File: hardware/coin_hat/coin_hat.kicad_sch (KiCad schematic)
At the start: 45 parts, among them J1 Pi 40-pin (bottom side), J10 Coin sensor, J11 Aux header, J12 Aux 12V switched, J2 Belt motor, J3 Feeder motor, J4 Diverter motor, J5 12 V in 5.5/2.1, J6 LED ring (WS2812), J7 Key light 12V switched, J8 Home: diverter, J9 Home: feeder, Q1 AO3400, Q2 AO3400, Q3 AO3400, U1 Raspberry Pi Pico, U2 TMC2209 StepStick, U3 TMC2209 StepStick, U4 TMC2209 StepStick, U5 12V->5V 5A module (Pololu D24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, U6 74AHCT1G125, U7 CAT24C32

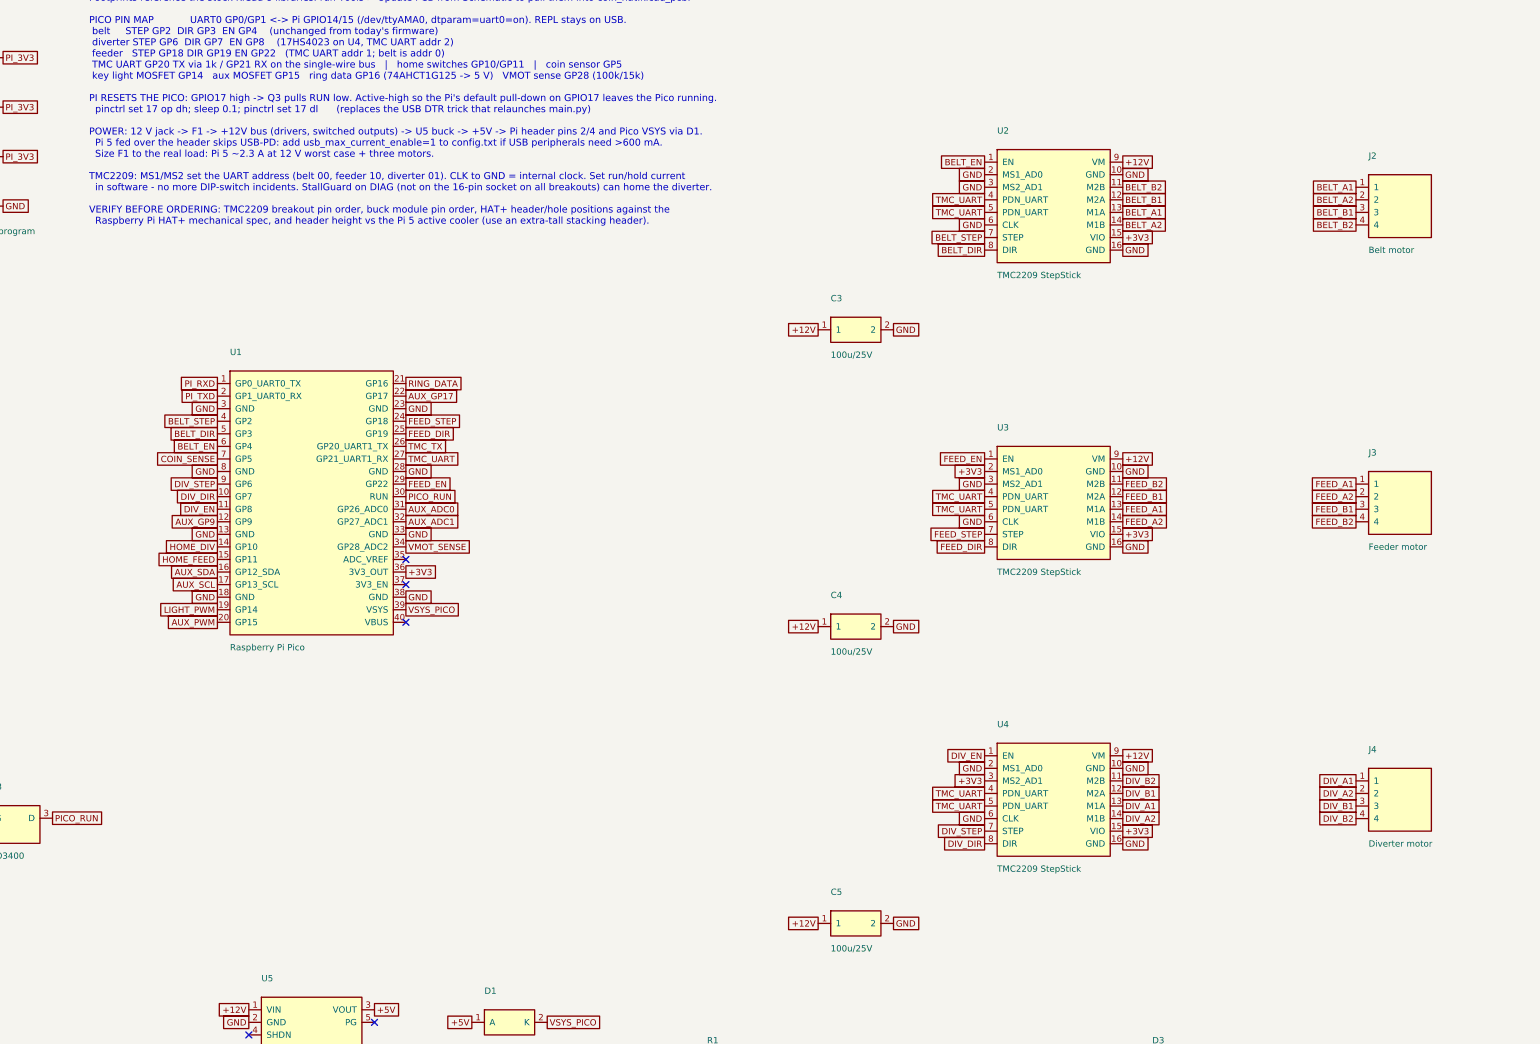
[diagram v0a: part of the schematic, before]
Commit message: coin_hat: driver sockets accept TMC2209 or A4988 via solder jumpers
Pins 4/5/6 of each StepStick socket were hard-wired for the TMC2209
(UART/UART/CLK->GND), which would hold an A4988 in SLEEP and leave MS3
on the UART bus. Add four solder jumpers per socket (MS1, MS2, pin4
UART-or-3V3, pin6 GND-or-pin5) and document both settings.

Co-Authored-By: Claude Opus 5 (1M context) <noreply@anthropic.com>
Claude-Session: https://claude.ai/code/session_01F7NoVCwbaSiu52WeHs72Ao
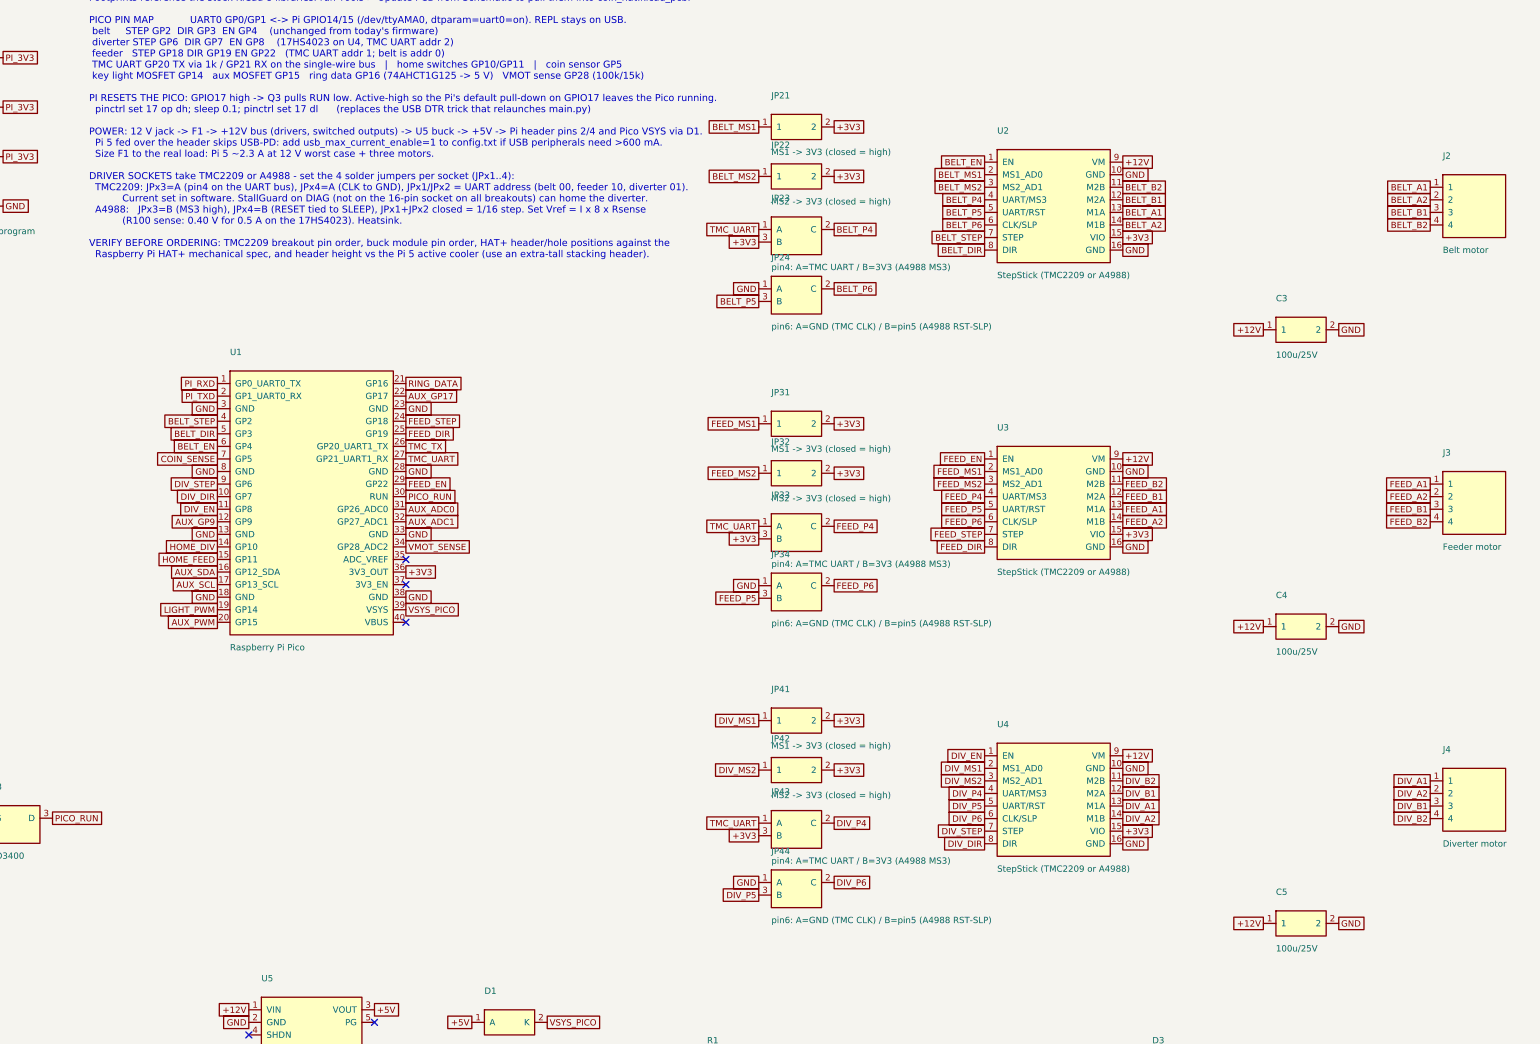
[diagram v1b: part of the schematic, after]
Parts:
- added JP21, JP31, JP41: MS1 -> 3V3 (closed = high), Jumper:SolderJumper-2_P1.3mm_Open_RoundedPad1.0x1.5mm, symbol coin_hat:Jumper
- added JP22, JP32, JP42: MS2 -> 3V3 (closed = high), Jumper:SolderJumper-2_P1.3mm_Open_RoundedPad1.0x1.5mm, symbol coin_hat:Jumper
- added JP23, JP33, JP43: pin4: A=TMC UART / B=3V3 (A4988 MS3), Jumper:SolderJumper-3_P1.3mm_Open_RoundedPad1.0x1.5mm, symbol coin_hat:Jumper3
- added JP24, JP34, JP44: pin6: A=GND (TMC CLK) / B=pin5 (A4988 RST-SLP), Jumper:SolderJumper-3_P1.3mm_Open_RoundedPad1.0x1.5mm, symbol coin_hat:Jumper3
- U2, U3, U4: value TMC2209 StepStick -> StepStick (TMC2209 or A4988)
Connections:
- net +3V3: now also JP21.2, JP22.2, JP23.3 (B), JP31.2, JP32.2, JP33.3 (B), JP41.2, JP42.2, JP43.3 (B); no longer U3.2 (MS1_AD0), U4.3 (MS2_AD1)
- net GND: now also JP24.1 (A), JP34.1 (A), JP44.1 (A); no longer U2.2 (MS1_AD0), U2.3 (MS2_AD1), U2.6 (CLK), U3.3 (MS2_AD1), U3.6 (CLK), U4.2 (MS1_AD0), U4.6 (CLK)
- net TMC_UART: now also JP23.1 (A), JP33.1 (A), JP43.1 (A); no longer U2.4 (PDN_UART), U2.5 (PDN_UART), U3.4 (PDN_UART), U3.5 (PDN_UART), U4.4 (PDN_UART), U4.5 (PDN_UART)
- new net BELT_MS1: JP21.1, U2.2 (MS1_AD0)
- new net BELT_MS2: JP22.1, U2.3 (MS2_AD1)
- new net BELT_P4: JP23.2 (C), U2.4 (UART/MS3)
- new net BELT_P5: JP24.3 (B), U2.5 (UART/RST)
- new net BELT_P6: JP24.2 (C), U2.6 (CLK/SLP)
- new net DIV_MS1: JP41.1, U4.2 (MS1_AD0)
- new net DIV_MS2: JP42.1, U4.3 (MS2_AD1)
- new net DIV_P4: JP43.2 (C), U4.4 (UART/MS3)
- new net DIV_P5: JP44.3 (B), U4.5 (UART/RST)
- new net DIV_P6: JP44.2 (C), U4.6 (CLK/SLP)
- new net FEED_MS1: JP31.1, U3.2 (MS1_AD0)
- new net FEED_MS2: JP32.1, U3.3 (MS2_AD1)
- new net FEED_P4: JP33.2 (C), U3.4 (UART/MS3)
- new net FEED_P5: JP34.3 (B), U3.5 (UART/RST)
- new net FEED_P6: JP34.2 (C), U3.6 (CLK/SLP)

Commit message: coin_hat: fix footprint names that don't resolve (Pico, 12V terminal blocks)
Co-Authored-By: Claude Opus 5 (1M context) <noreply@anthropic.com>
Claude-Session: https://claude.ai/code/session_01F7NoVCwbaSiu52WeHs72Ao
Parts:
- J12, J7: footprint TerminalBlock:TerminalBlock_bornier-2_P5.08mm -> Connector_JST:JST_XH_B2B-XH-A_1x02_P2.50mm_Vertical
- U1: footprint Module:RaspberryPi_Pico_SMD_TH -> Module:RaspberryPi_Pico_SMD_HandSolder

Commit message: coin_hat rev 1: servo diverter on its own buck, board runs lengthwise
The diverter is now the MG996R servo, not a stepper: drop the third
StepStick socket, its jumpers, motor connector and home switch, and add
a separate 12V->5-6V buck (U8) for a +SERVO rail, a 3-pin servo header
on GP6 (driven directly), 1000uF at the connector, a rail-live LED and
a GP27 rail sense. A dead servo rail with GP6 pulsing back-powers the
servo through its signal pin and looks like a signal fault.

The outline now runs along the Pi: 109 x 56.5, with a 44 mm overhang
past the SD end instead of 33.5 mm off the header edge. It also fixes
two rev 0 errors against the HAT+ spec: the header was 1.27 mm off in
both axes, and there was no notch for the Pi 5 camera/display FPCs.

Co-Authored-By: Claude Opus 5.5 <noreply@anthropic.com>
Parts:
- removed C5: 100u/25V, Capacitor_THT:CP_Radial_D8.0mm_P3.50mm, symbol coin_hat:Cap
- removed J4: Diverter motor, Connector_JST:JST_XH_B4B-XH-A_1x04_P2.50mm_Vertical, symbol coin_hat:Conn4
- removed J8: Home: diverter, Connector_JST:JST_XH_B2B-XH-A_1x02_P2.50mm_Vertical, symbol coin_hat:Conn2
- removed JP41: MS1 -> 3V3 (closed = high), Jumper:SolderJumper-2_P1.3mm_Open_RoundedPad1.0x1.5mm, symbol coin_hat:Jumper
- removed JP42: MS2 -> 3V3 (closed = high), Jumper:SolderJumper-2_P1.3mm_Open_RoundedPad1.0x1.5mm, symbol coin_hat:Jumper
- removed JP43: pin4: A=TMC UART / B=3V3 (A4988 MS3), Jumper:SolderJumper-3_P1.3mm_Open_RoundedPad1.0x1.5mm, symbol coin_hat:Jumper3
- removed JP44: pin6: A=GND (TMC CLK) / B=pin5 (A4988 RST-SLP), Jumper:SolderJumper-3_P1.3mm_Open_RoundedPad1.0x1.5mm, symbol coin_hat:Jumper3
- removed U4: StepStick (TMC2209 or A4988), Module:Pololu_Breakout-16_15.2x20.3mm, symbol coin_hat:StepStick
- added C6: 1000u/16V (at J4), Capacitor_THT:CP_Radial_D10.0mm_P5.00mm, symbol coin_hat:Cap
- added D5: green (servo rail live), LED_SMD:LED_0603_1608Metric, symbol coin_hat:LED
- added J4: Diverter servo (1 SIG / 2 V+ / 3 GND), Connector_PinHeader_2.54mm:PinHeader_1x03_P2.54mm_Vertical, symbol coin_hat:Conn3
- added R15: 1k, Resistor_SMD:R_0603_1608Metric, symbol coin_hat:Res
- added R16, R17: 10k, Resistor_SMD:R_0603_1608Metric, symbol coin_hat:Res
- added U8: 12V->5-6V 3A servo buck (Pololu D36V28F5 or F6), Connector_PinHeader_2.54mm:PinHeader_1x05_P2.54mm_Vertical, symbol coin_hat:Buck
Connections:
- net DIV_DIR is gone; now on net AUX_GP7: U1.10 (GP7)
- net +12V: now also U8.1 (VIN)
- net GND: now also C6.2, D5.2 (K), J4.3, R17.2, U8.2 (GND)
- net AUX_ADC1 renamed AUX_GP7
- net AUX_GP7: no longer U1.32 (GP27_ADC1)
- net DIV_EN: no longer names the net of U1.11 (GP8)
- net DIV_STEP renamed SERVO_PWM
- net SERVO_PWM: now also J4.1
- net HOME_DIV: no longer names the net of U1.14 (GP10)
- new net +SERVO: C6.1, J4.2, R15.1, R16.1, U8.3 (VOUT)
- new net SERVO_LED: D5.1 (A), R15.2
- new net SERVO_SENSE: R16.2, R17.1, U1.32 (GP27_ADC1)
- no-connect marks 29 -> 33
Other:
- note added: "Coin sorter HAT+ - rev 1 sketch (2026-09-27). Connectivity is by global labels; redraw with wires as you like. Footprints reference the stock KiCad 8 libraries: run Tools > Update PCB from Schematic to pull them into coin_hat.kicad_pcb. PICO PIN MAP UART0 GP0/GP1 <-> Pi GPIO14/15 (/dev/ttyAMA0, dtparam=uart0=on). REPL stays on USB. belt STEP GP2 DIR GP3 EN GP4 (unchanged from today's firmware) di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"
- note removed: "Coin sorter HAT+ - rev 0 sketch (2026-09-18). Connectivity is by global labels; redraw with wires as you like. Footprints reference the stock KiCad 8 libraries: run Tools > Update PCB from Schematic to pull them into coin_hat.kicad_pcb. PICO PIN MAP UART0 GP0/GP1 <-> Pi GPIO14/15 (/dev/ttyAMA0, dtparam=uart0=on). REPL stays on USB. belt STEP GP2 DIR GP3 EN GP4 (unchanged from today's firmware) di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"

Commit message: coin_hat: fix diode polarity and StepStick pinout, size board to fit
Checked with KiCad 9 (ERC, DRC, symbol pin vs footprint pad). Three
pin-numbering bugs carried over from rev 0 would have shipped broken:

- Diode symbols had the anode on pin 1; KiCad footprints put the
  cathode there. D3/D4 flybacks would short 12V to ground when the key
  light or aux output switched on, D1 would block the Pico's VSYS and
  the servo-rail LED would never light.
- The StepStick symbol numbered pins 1=EN..16=GND, but the
  Pololu_Breakout-16 footprint is 1=GND..16=DIR, so every driver pin,
  VMOT included, landed on the wrong pad.
- Neither Pololu buck matches the generic 1x5 footprint used for U5/U8
  (D24V50F5 has no PG, D36V28Fx has 6 pads). Flagged for redraw.

Packing the real courtyards (bucks are 17.8 x 20.3) showed the 44 mm
overhang cannot fit; 57 mm is the shortest clean floor plan. Board is
now 122 x 56.5 with that floor plan on User.Comments.

Co-Authored-By: Claude Opus 5.5 <noreply@anthropic.com>
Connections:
- net +12V: now also D3.1 (K), D4.1 (K), U2.8 (VM), U3.8 (VM); no longer D3.2, D4.2, U2.9 (VM), U3.9 (VM)
- net +3V3: now also U2.2 (VIO), U3.2 (VIO); no longer U2.15 (VIO), U3.15 (VIO)
- net +5V: now also D1.2 (A); no longer D1.1 (A)
- net AUX_SW: now also D4.2 (A); no longer D4.1
- net BELT_A1: now also U2.4 (M1A); no longer U2.13 (M1A)
- net BELT_A2: now also U2.3 (M1B); no longer U2.14 (M1B)
- net BELT_B1: now also U2.5 (M2A); no longer U2.12 (M2A)
- net BELT_B2: now also U2.6 (M2B); no longer U2.11 (M2B)
- net BELT_DIR: now also U2.16 (DIR); no longer U2.8 (DIR)
- net BELT_EN: now also U2.9 (EN); no longer U2.1 (EN)
- net BELT_MS1: now also U2.10 (MS1_AD0); no longer U2.2 (MS1_AD0)
- net BELT_MS2: now also U2.11 (MS2_AD1); no longer U2.3 (MS2_AD1)
- net BELT_P4: now also U2.12 (UART/MS3); no longer U2.4 (UART/MS3)
- net BELT_P5: now also U2.13 (UART/RST); no longer U2.5 (UART/RST)
- net BELT_P6: now also U2.14 (CLK/SLP); no longer U2.6 (CLK/SLP)
- net BELT_STEP: now also U2.15 (STEP); no longer U2.7 (STEP)
- net FEED_A1: now also U3.4 (M1A); no longer U3.13 (M1A)
- net FEED_A2: now also U3.3 (M1B); no longer U3.14 (M1B)
- net FEED_B1: now also U3.5 (M2A); no longer U3.12 (M2A)
- net FEED_B2: now also U3.6 (M2B); no longer U3.11 (M2B)
- net FEED_DIR: now also U3.16 (DIR); no longer U3.8 (DIR)
- net FEED_EN: now also U3.9 (EN); no longer U3.1 (EN)
- net FEED_MS1: now also U3.10 (MS1_AD0); no longer U3.2 (MS1_AD0)
- net FEED_MS2: now also U3.11 (MS2_AD1); no longer U3.3 (MS2_AD1)
- net FEED_P4: now also U3.12 (UART/MS3); no longer U3.4 (UART/MS3)
- net FEED_P5: now also U3.13 (UART/RST); no longer U3.5 (UART/RST)
- net FEED_P6: now also U3.14 (CLK/SLP); no longer U3.6 (CLK/SLP)
- net FEED_STEP: now also U3.15 (STEP); no longer U3.7 (STEP)
- net GND: now also D5.1 (K), U2.1 (GND), U2.7 (GND), U3.1 (GND), U3.7 (GND); no longer D5.2 (K), U2.10 (GND), U2.16 (GND), U3.10 (GND), U3.16 (GND)
- net LIGHT_SW: now also D3.2 (A); no longer D3.1
- net SERVO_LED: now also D5.2 (A); no longer D5.1 (A)
- net VSYS_PICO: now also D1.1 (K); no longer D1.2 (K)
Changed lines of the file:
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@@
   (paper "A3")
   (title_block (title "Coin sorter HAT+") (date "2026-09-27") (rev "1") (comment 1 "Pi 5 + Pico + 2x StepStick + MG996R servo on its own buck, 12V in") (comment 2 "Sketch generated for review - verify footprints and pin orders before ordering"))
-  (text "Coin sorter HAT+ - rev 1 sketch (2026-09-27). Connectivity is by global labels; redraw with wires as you like.\nFootprints reference the stock KiCad 8 libraries: run Tools > Update PCB from Schematic to pull them into coin_hat.kicad_pcb.\n\nPICO PIN MAP            UART0 GP0/GP1 <-> Pi GPIO14/15 (/dev/ttyAMA0, dtparam=uart0=on). REPL stays on USB.\n belt     STEP GP2  DIR GP3  EN GP4    (unchanged from today's firmware)\n diverter SERVO GP6 -> J4 signal, direct (no series R / pulldown). Servo rail sense GP27 (10k/10k)\n feeder   STEP GP18 DIR GP19 EN GP22   (TMC UART addr 1; belt is addr 0)\n TMC UART GP20 TX via 1k / GP21 RX on the single-wire bus   |   feeder home GP11   |   spare GP7 (J11), GP8, GP10   |   coin sensor GP5\n key light MOSFET GP14   aux MOSFET GP15   ring data GP16 (74AHCT1G125 -> 5 V)   VMOT sense GP28 (100k/15k)\n\nPI RESETS THE PICO: GPIO17 high -> Q3 pulls RUN low. Active-high so the Pi's default pull-down on GPIO17 leaves the Pico running.\n  pinctrl set 17 op dh; sleep 0.1; pinctrl set 17 dl      (replaces the USB DTR trick that relaunches main.py)\n\nPOWER: 12 V jack -> F1 -> +12V bus (drivers, switched outputs) -> U5 buck -> +5V -> Pi header pins 2/4 and Pico VSYS via D1.\n  Pi 5 fed over the header skips USB-PD: add usb_max_current_enable=1 to config.txt if USB peripherals need >600 mA.\n  SERVO: +12V -> U8 buck (own module, 5-6 V) -> +SERVO -> J4, C6 1000u AT the connector, D5 lights when the rail is live.\n  A dead servo rail + live GP6 back-powers the servo through its signal pin (twitches, never moves): check D5 / GP27 first.\n  Size F1 to the real load: Pi 5 ~2.3 A at 12 V worst case + two steppers + servo (1.4 A stall at 6 V = ~0.8 A at 12 V).\n\nDRIVER SOCKETS take TMC2209 or A4988 - set the 4 solder jumpers per socket (JPx1..4):\n  TMC2209: JPx3=A (pin4 on the UART bus), JPx4=A (CLK to GND), JPx1/JPx2 = UART address (belt 00, feeder 10).\n           Current set in software. StallGuard on DIAG is not on the 16-pin socket on all breakouts.\n  A4988:   JPx3=B (MS3 high), JPx4=B (RESET tied to SLEEP), JPx1+JPx2 closed = 1/16 step. Set Vref = I x 8 x Rsense\n           (R100 sense: 0.40 V for 0.5 A). Heatsink.\n\nVERIFY BEFORE ORDERING: TMC2209 breakout pin order, U5/U8 buck module pin order, HAT+ header/hole positions against the\n  Raspberry Pi HAT+ mechanical spec, and stacking-header height for 16 mm spacers (HAT+ spec, clears the Active Cooler)." (exclude_from_sim no) (at 105 5 0) (effects (font (size 1.4 1.4)) (justify left top)))
+  (text "Coin sorter HAT+ - rev 1 sketch (2026-09-27). Connectivity is by global labels; redraw with wires as you like.\nFootprints reference the stock KiCad 8 libraries: run Tools > Update PCB from Schematic to pull them into coin_hat.kicad_pcb.\n\nPICO PIN MAP            UART0 GP0/GP1 <-> Pi GPIO14/15 (/dev/ttyAMA0, dtparam=uart0=on). REPL stays on USB.\n belt     STEP GP2  DIR GP3  EN GP4    (unchanged from today's firmware)\n diverter SERVO GP6 -> J4 signal, direct (no series R / pulldown). Servo rail sense GP27 (10k/10k)\n feeder   STEP GP18 DIR GP19 EN GP22   (TMC UART addr 1; belt is addr 0)\n TMC UART GP20 TX via 1k / GP21 RX on the single-wire bus   |   feeder home GP11   |   spare GP7 (J11), GP8, GP10   |   coin sensor GP5\n key light MOSFET GP14   aux MOSFET GP15   ring data GP16 (74AHCT1G125 -> 5 V)   VMOT sense GP28 (100k/15k)\n\nPI RESETS THE PICO: GPIO17 high -> Q3 pulls RUN low. Active-high so the Pi's default pull-down on GPIO17 leaves the Pico running.\n  pinctrl set 17 op dh; sleep 0.1; pinctrl set 17 dl      (replaces the USB DTR trick that relaunches main.py)\n\nPOWER: 12 V jack -> F1 -> +12V bus (drivers, switched outputs) -> U5 buck -> +5V -> Pi header pins 2/4 and Pico VSYS via D1.\n  Pi 5 fed over the header skips USB-PD: add usb_max_current_enable=1 to config.txt if USB peripherals need >600 mA.\n  SERVO: +12V -> U8 buck (own module, 5-6 V) -> +SERVO -> J4, C6 1000u AT the connector, D5 lights when the rail is live.\n  A dead servo rail + live GP6 back-powers the servo through its signal pin (twitches, never moves): check D5 / GP27 first.\n  Size F1 to the real load: Pi 5 ~2.3 A at 12 V worst case + two steppers + servo (1.4 A stall at 6 V = ~0.8 A at 12 V).\n\nDRIVER SOCKETS take TMC2209 or A4988 - set the 4 solder jumpers per socket (JPx1..4):\n  TMC2209: JPx3=A (pin4 on the UART bus), JPx4=A (CLK to GND), JPx1/JPx2 = UART address (belt 00, feeder 10).\n           Current set in software. StallGuard on DIAG is not on the 16-pin socket on all breakouts.\n  A4988:   JPx3=B (MS3 high), JPx4=B (RESET tied to SLEEP), JPx1+JPx2 closed = 1/16 step. Set Vref = I x 8 x Rsense\n           (R100 sense: 0.40 V for 0.5 A). Heatsink.\n\nVERIFY BEFORE ORDERING: TMC2209 breakout pin order, U5/U8 buck footprints (generic 1x5 - neither Pololu module matches, redraw from the dimension diagram), HAT+ header/hole positions against the\n  Raspberry Pi HAT+ mechanical spec, and stacking-header height for 16 mm spacers (HAT+ spec, clears the Active Cooler)." (exclude_from_sim no) (at 105 5 0) (effects (font (size 1.4 1.4)) (justify left top)))
   (global_label "PI_3V3" (shape passive) (at 29.76 85.87 180) (fields_autoplaced yes)
     (effects (font (size 1.27 1.27)) (justify right))
